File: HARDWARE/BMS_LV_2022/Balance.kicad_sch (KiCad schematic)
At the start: 9 parts, among them Q3 ZXMN3F30FHTA

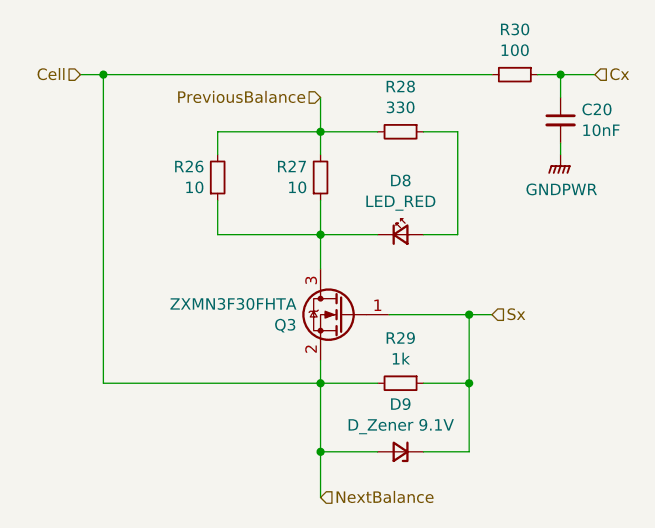
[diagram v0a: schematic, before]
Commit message: Autosport connector scheme updated
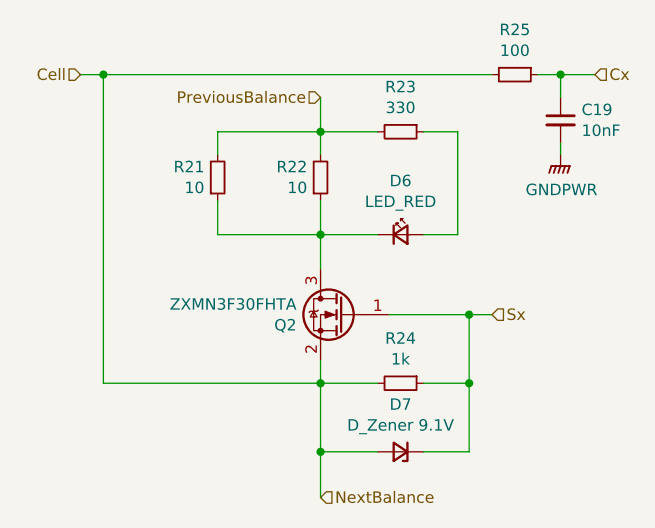
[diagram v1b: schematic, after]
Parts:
- renumbered C20 to C19, D8 to D6, D9 to D7, Q3 to Q2, R26 to R21, R27 to R22, R28 to R23, R29 to R24, R30 to R25
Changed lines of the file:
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@@
 		(on_board yes)
 		(dnp no)
-		(property "Reference" "R26"
+		(property "Reference" "R21"
 			(at 142.0368 101.7016 0)
 			(effects
@@
 		(on_board yes)
 		(dnp no)
-		(property "Reference" "R27"
+		(property "Reference" "R22"
 			(at 153.4668 101.7016 0)
 			(effects
@@
 		(on_board yes)
 		(dnp no)
-		(property "Reference" "R28"
+		(property "Reference" "R23"
 			(at 163.83 92.8116 90)
 			(effects
@@
 		(on_board yes)
 		(dnp no)
-		(property "Reference" "D8"
+		(property "Reference" "D6"
 			(at 163.83 103.251 0)
 			(effects
@@
 		(on_board yes)
 		(dnp no)
-		(property "Reference" "Q3"
+		(property "Reference" "Q2"
 			(at 152.273 119.2784 0)
 			(effects
@@
 		(on_board yes)
 		(dnp no)
-		(property "Reference" "R29"
+		(property "Reference" "R24"
 			(at 163.83 120.7516 90)
 			(effects
@@
 		(on_board yes)
 		(dnp no)
-		(property "Reference" "D9"
+		(property "Reference" "D7"
 			(at 163.83 128.0922 0)
 			(effects
@@
 		(on_board yes)
 		(dnp no)
-		(property "Reference" "R30"
+		(property "Reference" "R25"
 			(at 176.53 86.4616 90)
 			(effects
@@
 		(on_board yes)
 		(dnp no)
-		(property "Reference" "C20"
+		(property "Reference" "C19"
 			(at 183.9468 95.3516 0)
 			(effects
@@
 		(on_board yes)
 		(dnp no)
-		(property "Reference" "#PWR0113"
+		(property "Reference" "#PWR0112"
 			(at 181.61 105.41 0)
 			(effects
